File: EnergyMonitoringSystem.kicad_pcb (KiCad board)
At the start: 6 copper layers, 170 x 115 mm, 206 parts, among them J201 USB_C_Receptacle_USB2.0_16P, J202 Screw_Terminal_01x02, J401 Conn_02x05_Counter_Clockwise, J402 Conn_02x05_Counter_Clockwise, J403 Conn_02x08_Counter_Clockwise, J501 Screw_Terminal_01x02, J502 Screw_Terminal_01x02, J503 Screw_Terminal_01x02, J504 Screw_Terminal_01x02, J505 Screw_Terminal_01x02, J506 Screw_Terminal_01x02, J601 DM3AT-SF-PEJM5_40_, J602 Screw_Terminal_01x03, Q201 STL6N3LLH6, SW401 SW_Push, SW402 SW_Push, U201 USBLC6-2P6, U202 STEF05SGR, U203 TCPP01-M12, U301 LDLN025M12R, U302 ST1PS02CQTR, U303 ST1PS02CQTR, U304 LM2664M6_NOPB, U401 STM32F103RGT6, U402 BLUENRG-M2SA, U501 ADS131M08IRSNR, U502 TSV914AIDR, U503 TSV914AIDR, U504 TSV914AIDR, U601 EMIF06-MSD02N16, U602 ADM2565EBRNZ, Y401 16MHz, Y402 32.768KHz

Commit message: change in opAmp config
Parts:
- R406: value 47k -> 4k7
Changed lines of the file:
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@@
 			)
 		)
-		(property "Value" "47k"
+		(property "Value" "4k7"
 			(at 0 1.43 90)
 			(layer "F.Fab")
@@
 			)
 		)
-		(property "Datasheet" "https://www.vishay.com/doc?20043"
+		(property "Datasheet" "https://www.mouser.com/datasheet/2/447/PYu_SR_20105_RoHS_L_12-3461462.pdf"
 			(at 0 0 90)
 			(unlocked yes)
@@
 			)
 		)
-		(property "Distributor_Link" "https://www.mouser.com/ProductDetail/Vishay-Dale/CRCW060347K0FKEAHP?qs=k2%2FDWSARqgGdf8xU6XXKnw%3D%3D"
+		(property "Distributor_Link" "https://www.mouser.com/ProductDetail/YAGEO/SR0603FR-7T4K7L?qs=1mbolxNpo8e2BYIAXFrBnQ%3D%3D"
 			(at 0 0 90)
 			(unlocked yes)
@@
 			)
 		)
-		(property "Manufacturer_Name" "Vishay/Dale"
+		(property "Manufacturer_Name" "YAGEO"
 			(at 0 0 90)
 			(unlocked yes)
@@
 			)
 		)
-		(property "Manufacturer_Part_Number" "CRCW060347K0FKEAHP"
+		(property "Manufacturer_Part_Number" "SR0603FR-7T4K7L"
 			(at 0 0 90)
 			(unlocked yes)
@@
 	)
 	(segment
-		(start 128 49.4)
-		(end 127.5 48.9)
+		(start 127.5 48.9)
+		(end 127.5 47.5)
 		(width 0.2)
 		(layer "In2.Cu")
@@
 	)
 	(segment
-		(start 131.505 64.805)
-		(end 128 61.3)
+		(start 127.5 47.5)
+		(end 128.1 46.9)
 		(width 0.2)
 		(layer "In2.Cu")
@@
 	)
 	(segment
-		(start 145.3 46.9)
-		(end 146.54 45.66)
+		(start 131.505 70.195)
+		(end 131.505 64.805)
 		(width 0.2)
 		(layer "In2.Cu")
@@
 	)
 	(segment
-		(start 131.15 70.55)
-		(end 131.505 70.195)
+		(start 128 61.3)
+		(end 128 49.4)
 		(width 0.2)
 		(layer "In2.Cu")
@@
 	)
 	(segment
-		(start 128 61.3)
-		(end 128 49.4)
+		(start 131.15 70.55)
+		(end 131.505 70.195)
 		(width 0.2)
 		(layer "In2.Cu")
@@
 	)
 	(segment
-		(start 127.5 48.9)
-		(end 127.5 47.833654)
+		(start 131.505 64.805)
+		(end 128 61.3)
 		(width 0.2)
 		(layer "In2.Cu")
@@
 	)
 	(segment
-		(start 131.505 70.195)
-		(end 131.505 64.805)
+		(start 145.3 46.9)
+		(end 146.54 45.66)
 		(width 0.2)
 		(layer "In2.Cu")
@@
 	)
 	(segment
-		(start 127.5 47.833654)
-		(end 128.433654 46.9)
+		(start 128 49.4)
+		(end 127.5 48.9)
 		(width 0.2)
 		(layer "In2.Cu")
@@
 	)
 	(segment
-		(start 128.433654 46.9)
+		(start 128.1 46.9)
 		(end 145.3 46.9)
 		(width 0.2)

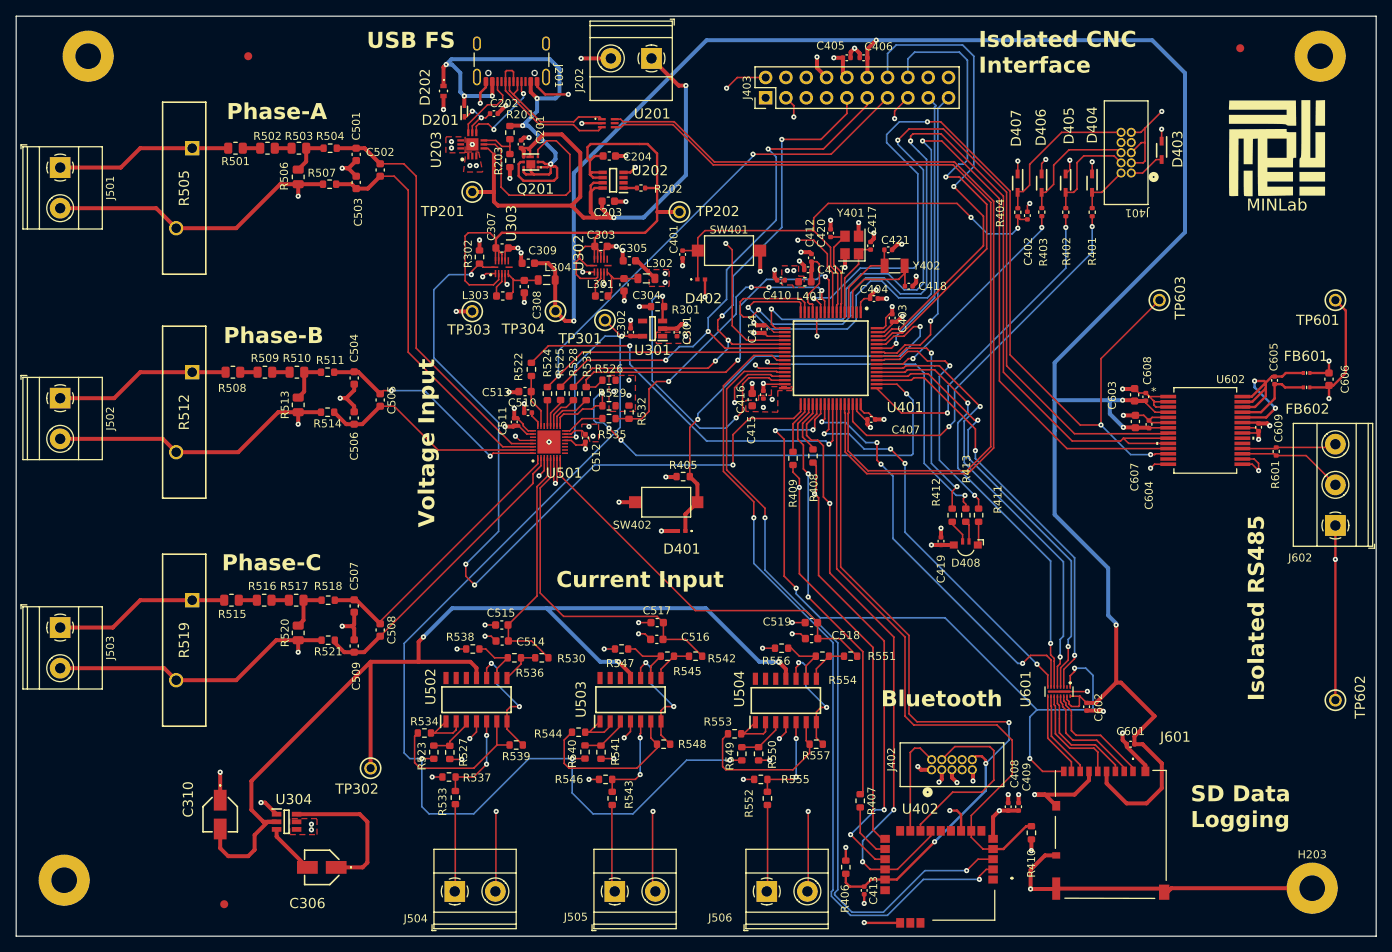
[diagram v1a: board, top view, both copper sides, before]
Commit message: update to OpAmp setup and bug fix
1. Fixed incorrect opamp connection
2. Improved RF connectivity for BLE
3. Fixed minor bugs
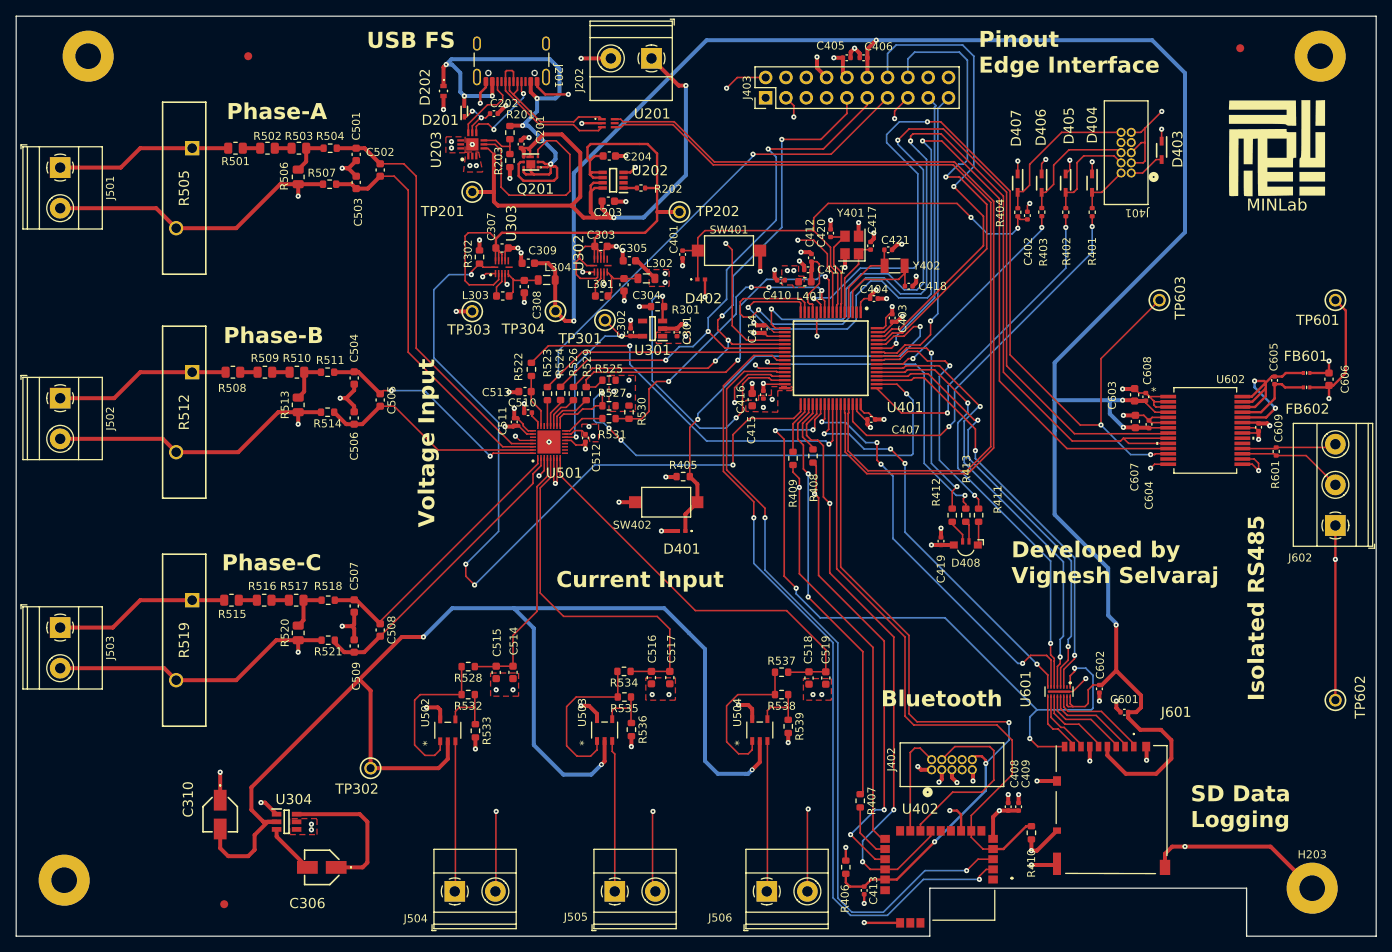
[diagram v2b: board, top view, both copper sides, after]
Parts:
- removed the R523 at (82.2, 130.0)
- removed the R527 at (84.2, 130.0)
- removed the R530 at (95.7, 118.2)
- removed R540, R549: 7k15, Resistor_SMD:R_0603_1608Metric
- removed R541, R550: 1k, Resistor_SMD:R_0603_1608Metric
- removed R542, R551: 2k, Resistor_SMD:R_0603_1608Metric
- removed R543, R544, R546, R548, R552, R553, R555, R557: 100k, Resistor_SMD:R_0603_1608Metric
- removed R545, R554: 62k, Resistor_SMD:R_0603_1608Metric
- removed R547, R556: 10k, Resistor_SMD:R_0603_1608Metric
- added R528: 2k, Resistor_SMD:R_0603_1608Metric, F.Cu at (86.5, 119.3)
- added R532: 15k, Resistor_SMD:R_0603_1608Metric, F.Cu at (86.5, 122.8)
- added R535: 15k, Resistor_SMD:R_0603_1608Metric, F.Cu at (106.0, 123.1)
- R533, R539: value 100k -> 10k
- R534, R537: value 100k -> 2k
- R536: value 62k -> 10k
- R538: value 10k -> 15k
- U502, U503, U504: value TSV914AIDR -> TSV911ILT; footprint EMS:TSV914AIDR-SOIC-14 -> EMS:TSV911ILT_SOT23-5
- moved R537 43.6 mm to (125.7, 120.0)
- moved R538 39.0 mm to (125.7, 122.8), turned to 180 degrees
- moved R539 34.1 mm to (126.5, 126.8), turned to -90 degrees
- moved R534 26.1 mm to (106.0, 119.9), turned to 180 degrees
- moved R536 17.2 mm to (106.9, 127.2), turned to -90 degrees
- moved R533 8.72 mm to (87.4, 127.3)
- moved C519 7.16 mm to (131.2, 120.7), turned to -90 degrees
- moved C517 7.05 mm to (111.7, 120.7), turned to -90 degrees
- moved C515 5.97 mm to (90.0, 120.0), turned to -90 degrees
- moved U502 5.24 mm to (83.9, 127.3)
- moved U503 4.99 mm to (103.5, 127.2)
- moved C518 4.94 mm to (129.1, 120.7), turned to -90 degrees
- moved U504 4.93 mm to (123.0, 127.2)
- moved C516 4.82 mm to (109.4, 120.7), turned to -90 degrees
- moved C514 4.15 mm to (92.1, 120.0), turned to -90 degrees
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- renumbered R524 to R523, R525 to R524, R526 to R525, R528 to R526, R529 to R527, R531 to R529, R532 to R530, R535 to R531
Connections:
- J504 pad 1: Net-(J504-Pin_1) -> /ADC/CT_PhaseA_IN
- J505 pad 1: Net-(J505-Pin_1) -> /ADC/CT_PhaseB_IN
- J506 pad 1: Net-(J506-Pin_1) -> /ADC/CT_PhaseC_IN
- R533 pad 1: Net-(U502-+INB) -> Net-(U502-IN-)
- R533 pad 2: Net-(J504-Pin_1) -> GND
- R534 pad 1: Net-(U502--INB) -> /ADC/I_Phase_B_P
- R534 pad 2: /ADC/VB_REF_A -> /ADC/CT_PhaseB_Amp_OUT
- R536 pad 1: Net-(U502--INC) -> Net-(U503-IN-)
- R536 pad 2: Net-(U502-OUTC) -> GND
- R537 pad 1: Net-(U502-+INB) -> /ADC/I_Phase_C_P
- R537 pad 2: GND -> /ADC/CT_PhaseC_Amp_OUT
- R538 pad 1: GND -> Net-(U504-IN-)
- R538 pad 2: Net-(U502--INC) -> /ADC/CT_PhaseC_Amp_OUT
- R539 pad 1: /ADC/LS_REF_A -> Net-(U504-IN-)
- R539 pad 2: Net-(U502--INB) -> GND
- U502 pad 1: /ADC/VB_REF_A -> /ADC/CT_PhaseA_Amp_OUT
- U502 pad 2: /ADC/VB_REF_A -> -DCDC_1
- U502 pad 3: Net-(U502-+INA) -> /ADC/CT_PhaseA_IN
- U502 pad 4: +DCDC_1 -> Net-(U502-IN-)
- U502 pad 5: Net-(U502-+INB) -> +DCDC_1
- U503 pad 1: /ADC/VB_REF_B -> /ADC/CT_PhaseB_Amp_OUT
- U503 pad 2: /ADC/VB_REF_B -> -DCDC_1
- U503 pad 3: Net-(U503-+INA) -> /ADC/CT_PhaseB_IN
- U503 pad 4: +DCDC_1 -> Net-(U503-IN-)
- U503 pad 5: Net-(U503-+INB) -> +DCDC_1
- U504 pad 1: /ADC/VB_REF_C -> /ADC/CT_PhaseC_Amp_OUT
- U504 pad 2: /ADC/VB_REF_C -> -DCDC_1
- U504 pad 3: Net-(U504-+INA) -> /ADC/CT_PhaseC_IN
- U504 pad 4: +DCDC_1 -> Net-(U504-IN-)
- U504 pad 5: Net-(U504-+INB) -> +DCDC_1
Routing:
- net +1V2: track 149.7 -> 23.3 mm, vias 5 -> 2
- net GND: track 434.1 -> 393.4 mm, vias 112 -> 109
- net -DCDC_1: track 138.2 -> 167.9 mm
- net Net-(U503--INB): track 20.9 -> 0.00 mm
- net /ADC/CT_PhaseB_Amp_OUT: track 0.00 -> 20.8 mm
- net /ADC/CT_PhaseA_Amp_OUT: track 0.00 -> 20.4 mm
- net Net-(U504--INB): track 20.3 -> 0.00 mm
- net Net-(U502--INB): track 20.2 -> 0.00 mm
- net /ADC/CT_PhaseB_IN: track 0.00 -> 19.4 mm
- net /ADC/CT_PhaseC_Amp_OUT: track 0.00 -> 19.1 mm
- net /ADC/CT_PhaseC_IN: track 0.00 -> 19.0 mm
- net /ADC/CT_PhaseA_IN: track 0.00 -> 18.8 mm
- net /ADC/LS_REF_A: track 15.9 -> 0.00 mm, vias 2 -> 0
- net /ADC/LS_REF_B: track 15.6 -> 0.00 mm, vias 2 -> 0
- net /ADC/LS_REF_C: track 15.4 -> 0.00 mm, vias 2 -> 0
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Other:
- outline, holes or cut-outs redrawn
- board text added: "Developed by Vignesh Selvaraj"
- board text added: "Pinout Edge Interface"
- board text removed: "Isolated CNC Interface"

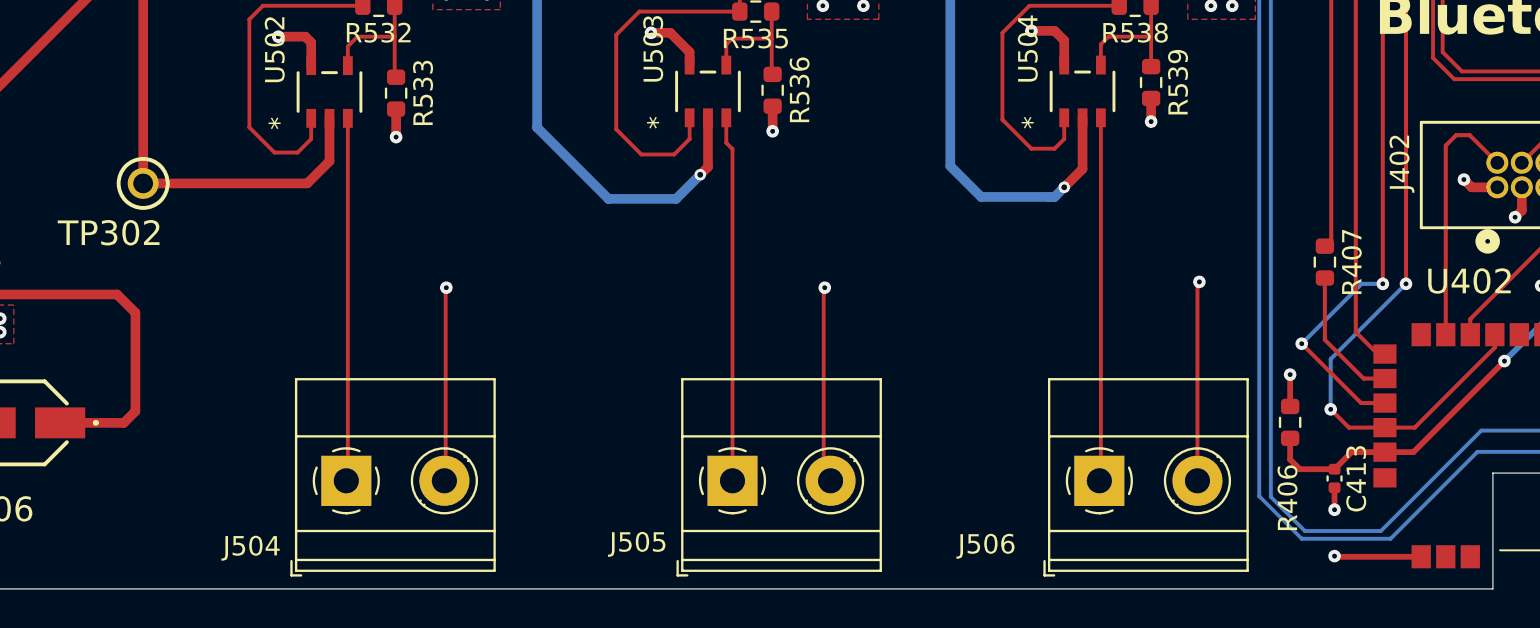
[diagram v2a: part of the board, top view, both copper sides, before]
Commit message: keep out zones for copper fills added
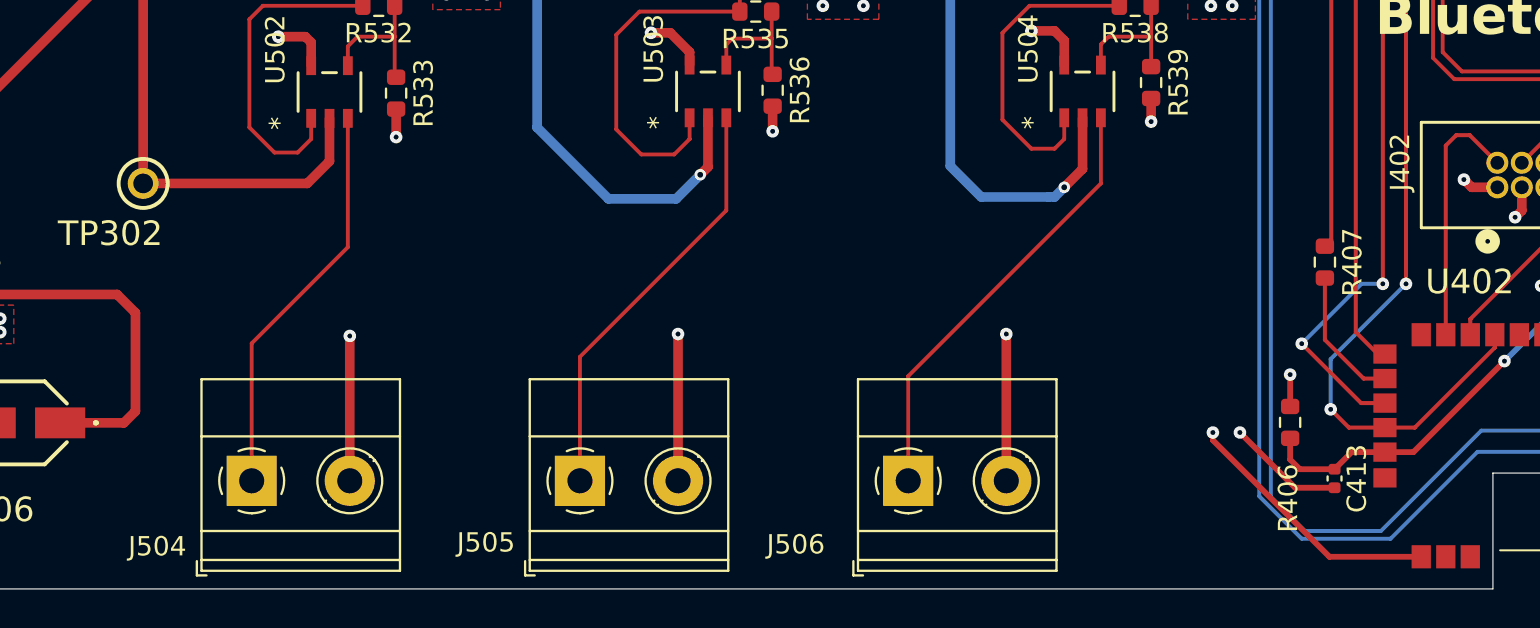
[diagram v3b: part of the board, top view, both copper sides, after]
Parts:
- moved J506 9.90 mm to (113.9, 147.4)
- moved J505 7.90 mm to (96.9, 147.4)
- moved J504 4.90 mm to (79.9, 147.4)
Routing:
- net GND: track 393.4 -> 399.7 mm
- net /ADC/CT_PhaseC_IN: track 19.0 -> 22.9 mm
- net /ADC/CT_PhaseB_IN: track 19.4 -> 21.9 mm
- net /ADC/CT_PhaseA_IN: track 18.8 -> 20.8 mm
